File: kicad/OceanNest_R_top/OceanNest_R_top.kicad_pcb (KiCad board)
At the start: 2 copper layers, 103.4 x 85.9 mm, 20 parts, among them SW21 SW_PUSH, SW22 SW_PUSH, SW23 SW_PUSH, SW24 SW_PUSH, SW25 SW_PUSH, SW26 SW_PUSH, SW27 SW_PUSH, SW28 SW_PUSH, SW29 SW_PUSH, SW30 SW_PUSH, SW31 SW_PUSH, SW32 SW_PUSH, SW33 SW_PUSH, SW34 SW_PUSH, SW35 SW_PUSH, SW36 SW_PUSH

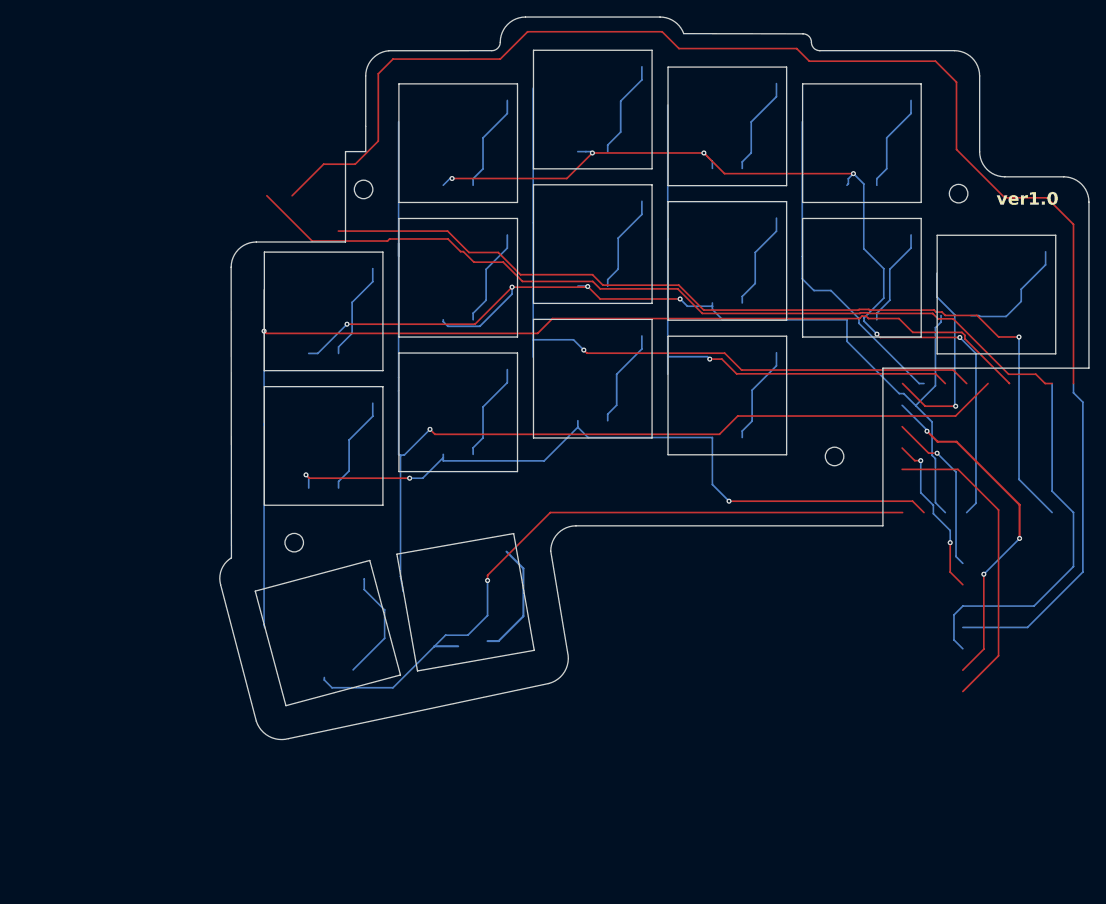
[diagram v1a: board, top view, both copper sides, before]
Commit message: feat: update PCB and schematic files for OceanNest project, including new components and layout adjustments
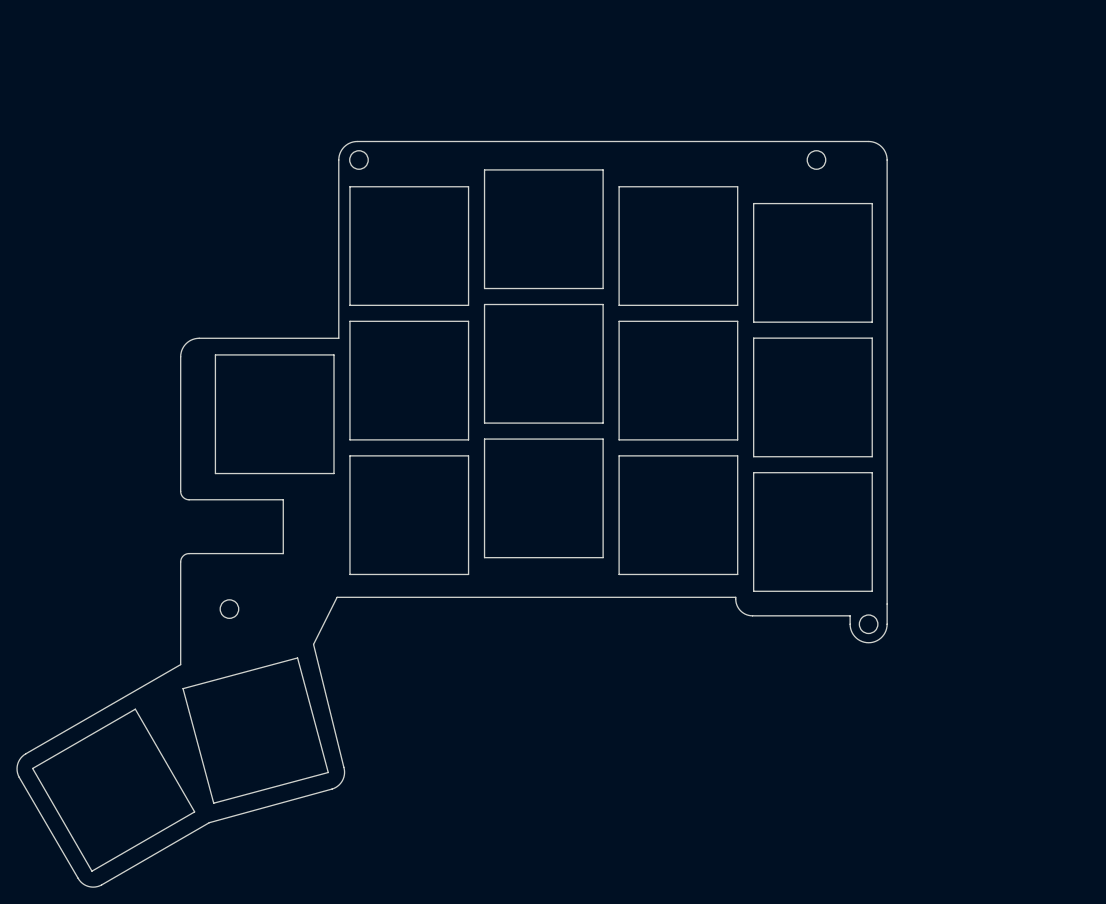
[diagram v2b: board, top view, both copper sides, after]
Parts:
- removed the Ref** at (115.8, 67.5)
- removed the Ref** at (171.8, 99.2)
- removed the Ref** at (107.5, 109.5)
- removed the Ref** at (186.5, 68.0)
- removed SW36: SW_PUSH, isw-kbd:SW_Hole_CherryMX_16mm
- added Ref**: Val**, isw-kbd:M2_ScrewHole, F.Cu at (175.8, 119.2)
- added Ref**: Val**, isw-kbd:M2_ScrewHole, F.Cu at (169.6, 64.0)
- added Ref**: Val**, isw-kbd:M2_ScrewHole, F.Cu at (115.2, 64.0)
- added Ref**: Val**, isw-kbd:M2_ScrewHole, F.Cu at (99.8, 117.4)
- SW21, SW22, SW23, SW24, SW25, SW26, SW27, SW28, SW29, SW30, SW31, SW32, SW33, SW34, SW35: value SW_PUSH -> SW_Push
- moved SW34 86.8 mm to (86.0, 138.9), turned to 30 degrees
- moved SW30 74.6 mm to (121.2, 106.2)
- moved SW33 31.9 mm to (169.2, 108.2)
- moved SW32 28.9 mm to (153.2, 106.2)
- moved SW31 26.9 mm to (137.2, 104.2)
- moved SW22 15.4 mm to (137.2, 72.2)
- moved SW23 15.4 mm to (153.2, 74.2)
- moved SW24 15.4 mm to (169.2, 76.2)
- moved SW27 15.4 mm to (137.2, 88.2)
- moved SW28 15.4 mm to (153.2, 90.2)
- moved SW29 15.4 mm to (169.2, 92.2)
- moved SW35 14.4 mm to (102.9, 131.8)
- moved SW21 13.5 mm to (121.2, 74.2)
- moved SW25 13.5 mm to (105.2, 94.2)
- moved SW26 13.5 mm to (121.2, 90.2)
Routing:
- net VCC: track 178.7 -> 0.00 mm
- net GND: track 146.8 -> 0.00 mm
- net col0: track 133.3 -> 0.00 mm, vias 1 -> 0
- net col1: track 131.5 -> 0.00 mm, vias 1 -> 0
- net row1: track 121.8 -> 0.00 mm, vias 4 -> 0
- net row0: track 111.4 -> 0.00 mm, vias 6 -> 0
- net data: track 108.7 -> 0.00 mm, vias 1 -> 0
- net row2: track 87.0 -> 0.00 mm, vias 3 -> 0
- net col2: track 85.7 -> 0.00 mm, vias 1 -> 0
- net row3: track 83.8 -> 0.00 mm, vias 1 -> 0
- net col3: track 66.3 -> 0.00 mm, vias 1 -> 0
- net NCS: track 41.4 -> 0.00 mm, vias 3 -> 0
- net col4: track 38.6 -> 0.00 mm
- net SCLK: track 36.8 -> 0.00 mm
- net col5: track 24.8 -> 0.00 mm, vias 1 -> 0
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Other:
- board size 103.4 x 85.9 mm -> 103.5 x 88.7 mm
- board text removed: "c0"
- board text removed: "ver1.0"

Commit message: feat: add new OceanNest_L and OceanNest_R PCB and project files for enhanced design capabilities
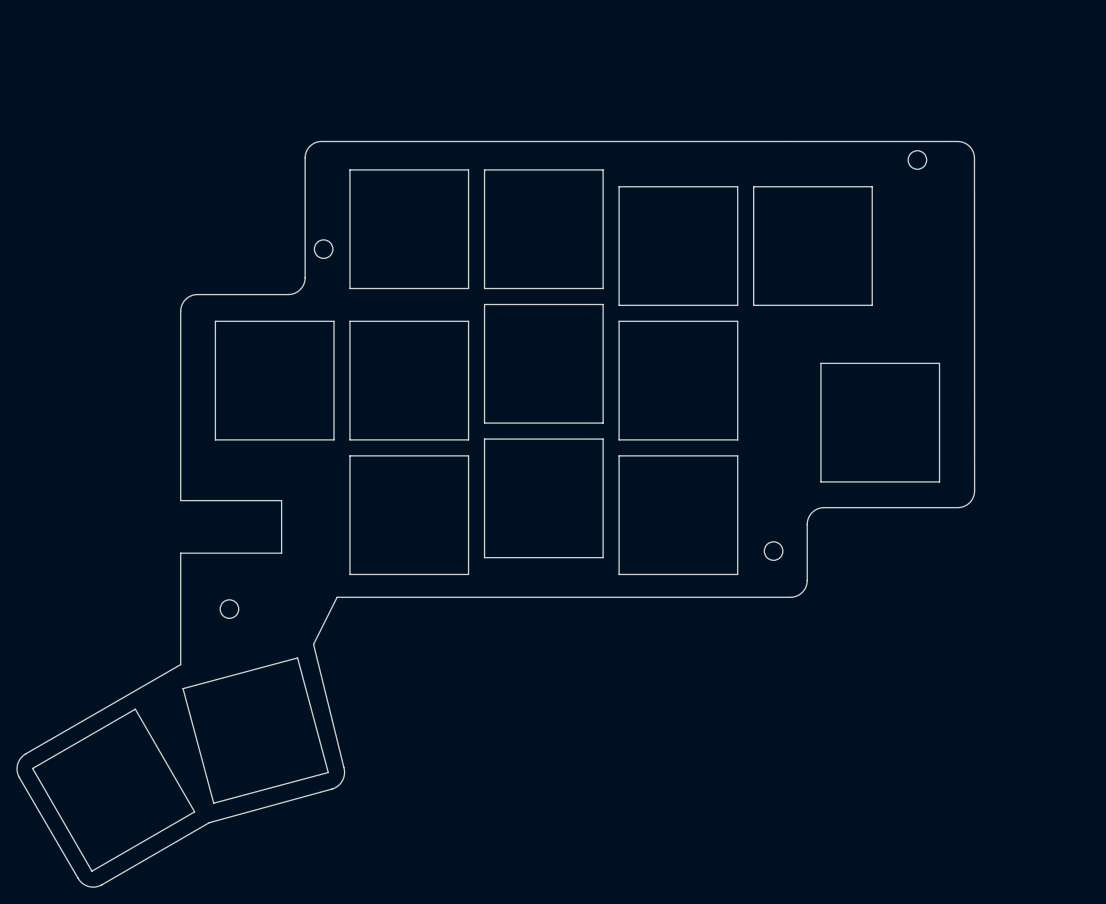
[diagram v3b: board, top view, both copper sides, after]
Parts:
- removed Ref** (x3): Val**, isw-kbd:M2_ScrewHole
- removed the SW33 at (169.2, 108.2)
- added hole2: Val**, kbd_Hole:m2_Screw_Hole, F.Cu at (164.5, 110.5)
- added hole2: Val**, kbd_Hole:m2_Screw_Hole, F.Cu at (181.6, 64.0)
- added hole2: Val**, kbd_Hole:m2_Screw_Hole, F.Cu at (111.0, 74.6)
- hole1: renamed from Ref**; footprint isw-kbd:M2_ScrewHole -> kbd_Hole:m2_Screw_Hole
- moved SW29 8.54 mm to (177.2, 95.2)
- moved SW25 4.00 mm to (105.2, 90.2)
- moved SW21 2.00 mm to (121.2, 72.2)
- moved SW24 2.00 mm to (169.2, 74.2)
- renumbered SW34 to SW33, SW35 to SW34
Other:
- board size 103.5 x 88.7 mm -> 113.9 x 88.7 mm
